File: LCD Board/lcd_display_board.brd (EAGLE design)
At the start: 47.2 x 39.3 mm, 26 parts, among them U1 ATMEGA328P_TQFP, Y1 16MHz

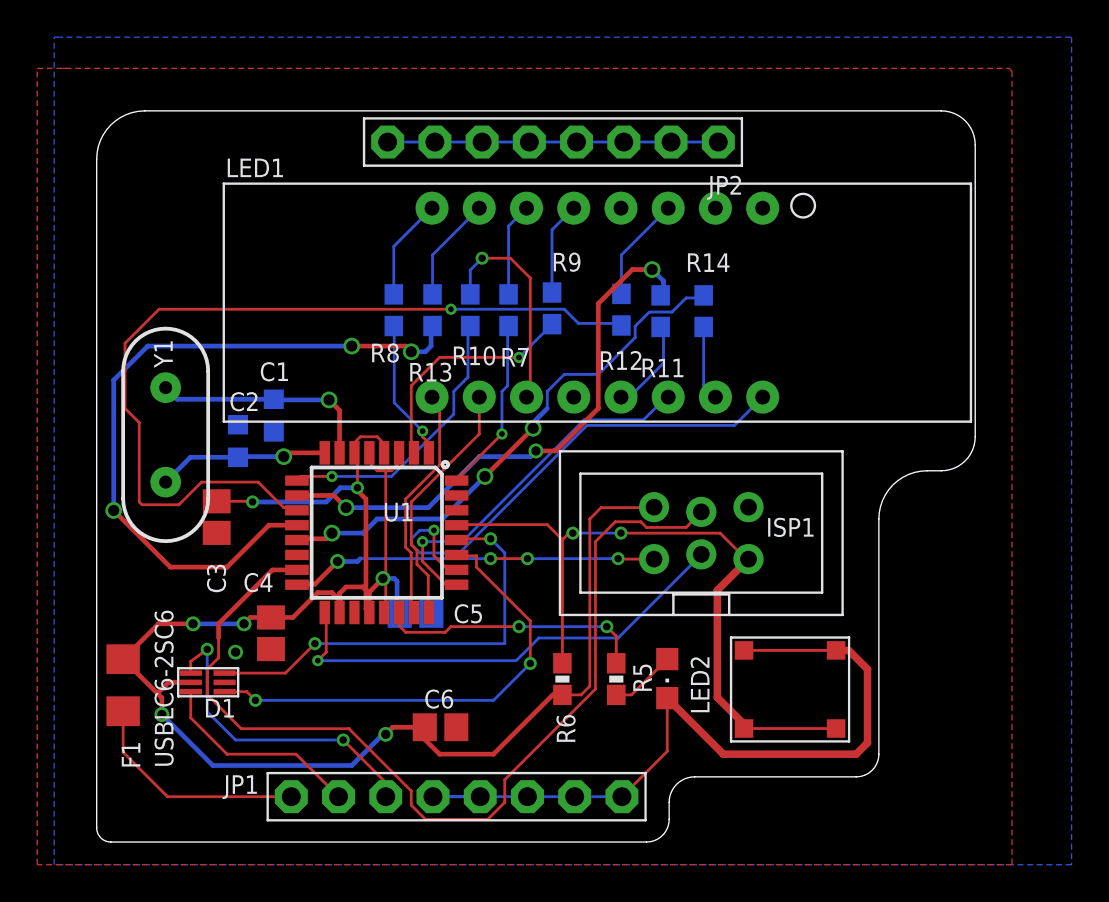
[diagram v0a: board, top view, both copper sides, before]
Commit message: fcc schematic mostly done
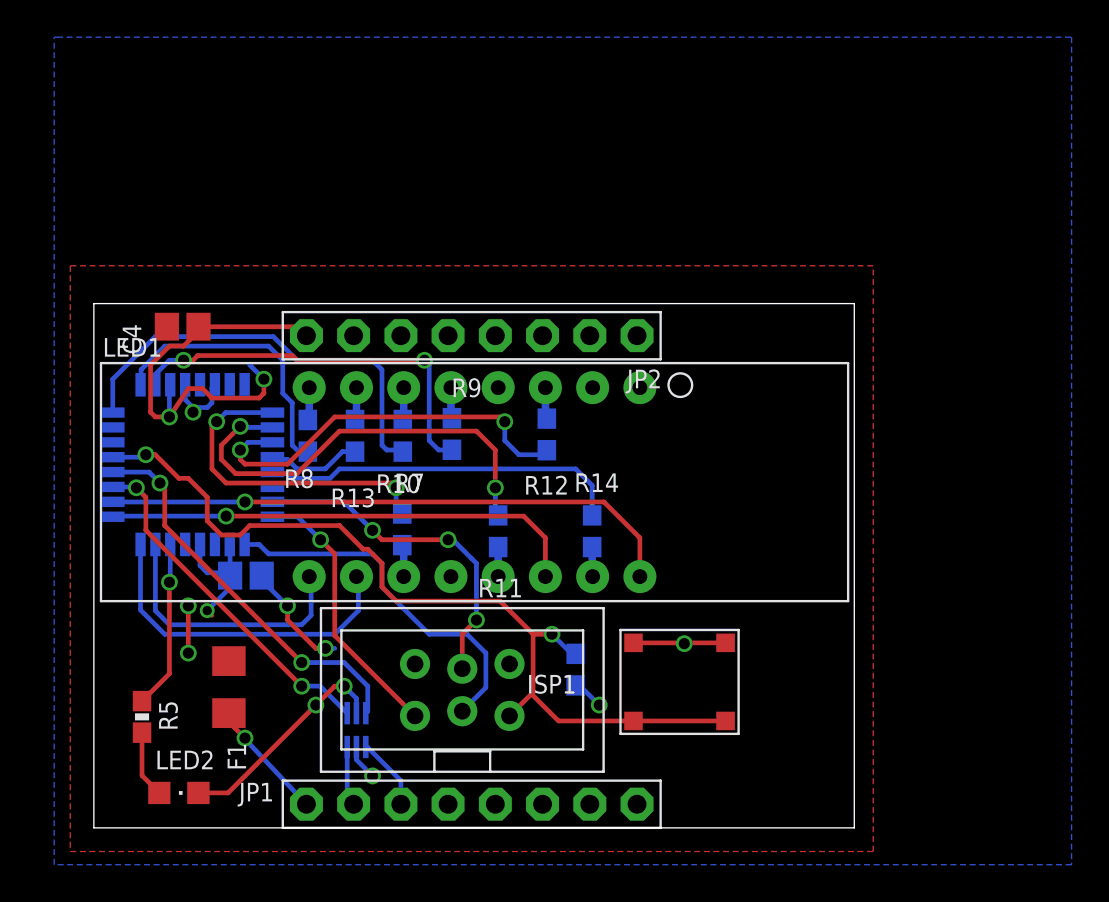
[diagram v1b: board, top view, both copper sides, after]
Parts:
- removed C1, C2: 22pF, adafruit:C0603K
- removed C5: 0.1uF, adafruit:C0805
- removed C6: 1uF, adafruit:C0805
- removed Y1: 16MHz, SparkFun-FreqCtrl:HC49US
- moved LED2 27.0 mm to (4.57, 1.88), turned to 270 degrees
- moved R5 25.6 mm to (2.59, 5.97)
- moved C4 17.2 mm to (4.78, 26.9), turned to 0 degrees
- moved ISP1 15.4 mm to (19.8, 7.42)
- moved R11 14.7 mm to (21.7, 16.0)
- moved R14 13.3 mm to (26.8, 16.0)
- moved R10 12.3 mm to (16.6, 16.1), turned to 270 degrees
- moved LED1 11.7 mm to (20.5, 18.6)
- moved JP2 11.3 mm to (20.3, 26.5)
- moved U1 10.6 mm to (5.31, 19.5), flipped to the bottom
- moved R7 8.83 mm to (16.6, 21.1)
- moved R9 8.64 mm to (19.3, 21.2)
- moved D1 8.40 mm to (14.1, 5.26), flipped to the bottom, turned to 180 degrees
- moved R8 8.19 mm to (11.5, 21.1)
- moved R13 7.94 mm to (14.0, 21.1)
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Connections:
- removed net +5V: C3.1, C4.1, C5.1, C6.1, D1.P$5, F1.1, ISP1.2, R6.2, U1.18, U1.20, U1.4, U1.6
- removed net N$1: C1.1, U1.7, Y1.2
- removed net N$2: C2.1, U1.8, Y1.1
- new net +3.3V: C3.1, C4.1, D1.P$5, F1.1, R6.2, U1.18, U1.20, U1.4, U1.6
- new net VCC: ISP1.2
- net GND: no longer C1.2, C2.2, C5.2, C6.2
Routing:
- net +5V: track 87.2 -> 0.00 mm, vias 7 -> 0
- net MOSI: track 52.3 -> 18.3 mm, vias 0 -> 3
- net N$15: track 38.3 -> 5.09 mm, vias 3 -> 0
- net N$14: track 46.4 -> 21.6 mm, vias 1 -> 2
- net GND: track 71.0 -> 49.2 mm, vias 1 -> 9
- net +3.3V: track 0.00 -> 15.6 mm, vias 0 -> 4
- net N$9: track 9.49 -> 23.3 mm, vias 1 -> 0
- net N$17: track 17.0 -> 3.91 mm, vias 2 -> 0
- net N$1: track 12.1 -> 0.00 mm, vias 1 -> 0
- net SEGD: track 11.7 -> 1.77 mm, vias 1 -> 0
- net N$2: track 9.21 -> 0.00 mm, vias 1 -> 0
- net N$16: track 28.5 -> 19.5 mm, vias 3 -> 0
- net N$11: track 12.6 -> 21.4 mm, vias 1 -> 2
- net ATM_RESET: track 38.8 -> 47.3 mm
- net N$6: track 11.1 -> 3.18 mm
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- added copper zone on layer 1, net +3.3V
- removed copper zone on layer 1, net GND
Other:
- board size 47.2 x 39.3 mm -> 40.9 x 28.2 mm

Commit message: cleaned up silk screens
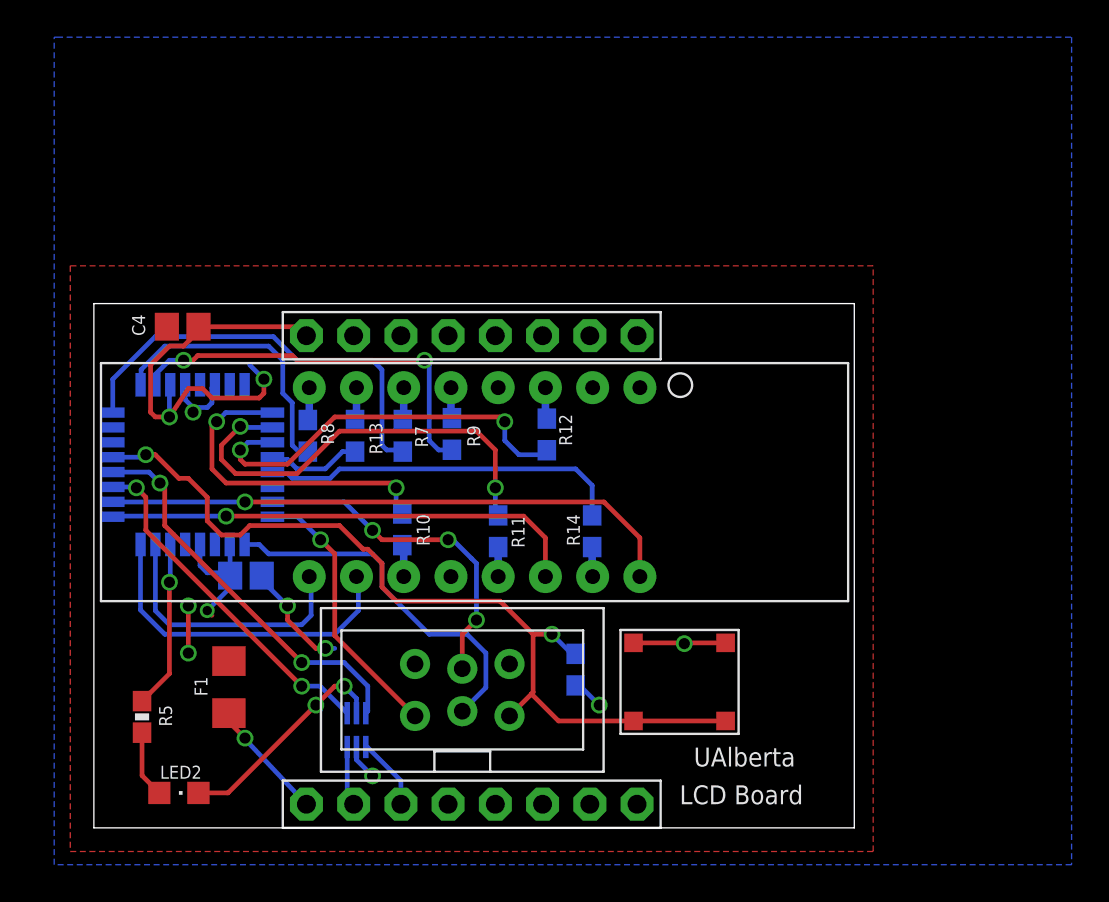
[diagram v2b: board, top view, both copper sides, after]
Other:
- board text added: "LCD Board"
- board text added: "UAlberta"
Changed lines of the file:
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@@
 <wire x1="40.894" y1="28.194" x2="0" y2="28.194" width="0" layer="20"/>
 <wire x1="0" y1="28.194" x2="0" y2="0" width="0" layer="20"/>
+<text x="32.258" y="3.302" size="1.016" layer="21" ratio="18">UAlberta</text>
+<text x="31.496" y="1.27" size="1.016" layer="21" ratio="18">LCD Board</text>
 </plain>
 <attributes>
@@
 <elements>
 <element name="C3" library="adafruit" package="C0805" value="1uF" x="8.1788" y="13.5636" smashed="yes" rot="MR180">
-<attribute name="NAME" x="10.6426" y="14.0716" size="1" layer="26" rot="MR180"/>
-<attribute name="VALUE" x="8.509" y="16.1544" size="1" layer="28" rot="MR180"/>
+<attribute name="NAME" x="8.8646" y="15.3416" size="0.7" layer="26" ratio="15" rot="MR180"/>
 </element>
 <element name="C4" library="adafruit" package="C0805" value="0.1uF" x="4.7752" y="26.9494" smashed="yes">
-<attribute name="NAME" x="1.5494" y="27.1018" size="1" layer="25" rot="R270"/>
-<attribute name="VALUE" x="7.8486" y="26.1874" size="1" layer="27" rot="R90"/>
+<attribute name="NAME" x="2.0574" y="27.6098" size="0.7" layer="25" ratio="15" rot="R270"/>
 </element>
 <element name="D1" library="USBLC6-2SC6" package="USBLC6-2SC6" value="USBLC6-2SC6" x="14.1224" y="5.2578" smashed="yes" rot="MR180">
-<attribute name="NAME" x="13.2334" y="6.7818" size="1" layer="22" rot="MR270"/>
-<attribute name="VALUE" x="18.0594" y="2.413" size="1" layer="22" rot="MR0"/>
+<attribute name="NAME" x="13.2334" y="6.0198" size="0.7" layer="22" ratio="15" rot="MR270"/>
 </element>
 <element name="F1" library="polyfuse" package="1206" value="" x="7.2644" y="7.5692" smashed="yes" rot="R270">
-<attribute name="NAME" x="7.1882" y="4.572" size="1" layer="25" rot="R270"/>
+<attribute name="NAME" x="5.4102" y="8.128" size="0.7" layer="25" ratio="15" rot="R270"/>
 <attribute name="VALUE" x="5.7404" y="8.9662" size="0.4064" layer="27" rot="R270"/>
 </element>
-<element name="ISP1" library="adafruit" package="AVRISP-BOX" value="AVRISP-BOX" x="19.812" y="7.4168" smashed="yes" rot="R90">
-<attribute name="NAME" x="25.9604" y="8.2268" size="1" layer="25" rot="R180"/>
-</element>
-<element name="LED1" library="SparkFun-Displays" package="7-SEGMENT-4DIGIT-YOUNGSUN" value="7-SEGMENT-4DIGIT-YOUNGSUN" x="20.4724" y="18.5928" smashed="yes">
-<attribute name="NAME" x="0.4724" y="25.3388" size="1" layer="25"/>
-<attribute name="VALUE" x="39.177" y="11.7084" size="1" layer="27" rot="R180"/>
-</element>
+<element name="ISP1" library="adafruit" package="AVRISP-BOX" value="AVRISP-BOX" x="19.812" y="7.4168" smashed="yes" rot="R90"/>
+<element name="LED1" library="SparkFun-Displays" package="7-SEGMENT-4DIGIT-YOUNGSUN" value="7-SEGMENT-4DIGIT-YOUNGSUN" x="20.4724" y="18.5928" smashed="yes"/>
 <element name="LED2" library="adafruit" package="CHIPLED_0805" value="" x="4.572" y="1.8796" smashed="yes" rot="R270">
-<attribute name="NAME" x="3.302" y="3.1496" size="1" layer="25"/>
+<attribute name="NAME" x="3.556" y="2.6416" size="0.7" layer="25" ratio="15"/>
 <attribute name="VALUE" x="3.302" y="-0.6604" size="1.27" layer="27"/>
 </element>
 <element name="R10" library="SparkFun-Resistors" package="0603-RES" value="80 Ohm" x="16.5862" y="16.0528" smashed="yes" rot="MR270">
-<attribute name="NAME" x="15.1638" y="18.0086" size="1" layer="25" font="vector" ratio="11"/>
-<attribute name="VALUE" x="17.272" y="17.0688" size="1" layer="27" font="vector" ratio="11" rot="R270"/>
+<attribute name="NAME" x="18.0594" y="15.1638" size="0.7" layer="25" font="vector" ratio="15" rot="R90"/>
 </element>
 <element name="R11" library="SparkFun-Resistors" package="0603-RES" value="80 Ohm" x="21.7424" y="15.9512" smashed="yes" rot="MR270">
-<attribute name="NAME" x="20.6502" y="12.3952" size="1" layer="25" font="vector" ratio="11"/>
-<attribute name="VALUE" x="20.2946" y="19.8628" size="1" layer="27" font="vector" ratio="11" rot="R270"/>
+<attribute name="NAME" x="23.1648" y="15.0622" size="0.7" layer="25" font="vector" ratio="15" rot="R90"/>
 </element>
 <element name="R12" library="SparkFun-Resistors" package="0603-RES" value="80 Ohm" x="24.3586" y="21.1582" smashed="yes" rot="MR90">
-<attribute name="NAME" x="25.5524" y="18.923" size="1" layer="25" font="vector" ratio="11" rot="R180"/>
-<attribute name="VALUE" x="23.5204" y="19.5326" size="1" layer="27" font="vector" ratio="11" rot="R90"/>
+<attribute name="NAME" x="25.019" y="22.2504" size="0.7" layer="25" font="vector" ratio="15" rot="R270"/>
 </element>
 <element name="R13" library="SparkFun-Resistors" package="0603-RES" value="80 Ohm" x="14.0462" y="21.082" smashed="yes" rot="MR90">
-<attribute name="NAME" x="12.7254" y="17.2466" size="1" layer="25" font="vector" ratio="11"/>
-<attribute name="VALUE" x="13.5128" y="20.066" size="1" layer="27" font="vector" ratio="11" rot="R90"/>
+<attribute name="NAME" x="15.5194" y="20.0914" size="0.7" layer="25" font="vector" ratio="15" rot="R90"/>
 </element>
 <element name="R14" library="SparkFun-Resistors" package="0603-RES" value="80 Ohm" x="26.797" y="15.9512" smashed="yes" rot="MR270">
-<attribute name="NAME" x="25.8318" y="18.0594" size="1" layer="25" font="vector" ratio="11"/>
-<attribute name="VALUE" x="27.6352" y="18.034" size="1" layer="27" font="vector" ratio="11" rot="R270"/>
+<attribute name="NAME" x="26.1366" y="15.1638" size="0.7" layer="25" font="vector" ratio="15" rot="R90"/>
 </element>
 <element name="R5" library="SparkFun-Resistors" package="0603-RES" value="1k" x="2.5908" y="5.969" smashed="yes" rot="R270">
-<attribute name="NAME" x="3.5052" y="6.858" size="1" layer="25" font="vector" ratio="11" rot="R270"/>
-<attribute name="VALUE" x="2.0574" y="3.937" size="1" layer="27" font="vector" ratio="11" rot="R270"/>
+<attribute name="NAME" x="3.5052" y="6.604" size="0.7" layer="25" font="vector" ratio="15" rot="R270"/>
 </element>
 <element name="R6" library="SparkFun-Resistors" package="0603-RES" value="10k" x="25.908" y="8.509" smashed="yes" rot="MR270">
-<attribute name="NAME" x="26.2128" y="6.6548" size="1" layer="26" font="vector" ratio="11" rot="MR270"/>
-<attribute name="VALUE" x="27.9654" y="8.4582" size="1" layer="28" font="vector" ratio="11" rot="MR270"/>
+<attribute name="NAME" x="24.9428" y="9.4488" size="0.7" layer="26" font="vector" ratio="15" rot="MR270"/>
 </element>
 <element name="R7" library="SparkFun-Resistors" package="0603-RES" value="80 Ohm" x="16.6116" y="21.082" smashed="yes" rot="MR90">
-<attribute name="NAME" x="17.8054" y="19.05" size="1" layer="25" font="vector" ratio="11" rot="R180"/>
-<attribute name="VALUE" x="16.0782" y="20.066" size="1" layer="27" font="vector" ratio="11" rot="R90"/>
+<attribute name="NAME" x="17.272" y="21.6154" size="0.7" layer="25" font="vector" ratio="15" rot="R270"/>
 </element>
 <element name="R8" library="SparkFun-Resistors" package="0603-RES" value="80 Ohm" x="11.5062" y="21.082" smashed="yes" rot="MR90">
-<attribute name="NAME" x="11.8618" y="19.2786" size="1" layer="25" font="vector" ratio="11" rot="R180"/>
-<attribute name="VALUE" x="10.3632" y="20.066" size="1" layer="27" font="vector" ratio="11" rot="R90"/>
+<attribute name="NAME" x="12.2174" y="21.7678" size="0.7" layer="25" font="vector" ratio="15" rot="R270"/>
 </element>
 <element name="R9" library="SparkFun-Resistors" package="0603-RES" value="80 Ohm" x="19.2532" y="21.1836" smashed="yes" rot="MR90">
-<attribute name="NAME" x="19.2278" y="23.1648" size="1" layer="25" font="vector" ratio="11"/>
-<attribute name="VALUE" x="18.7198" y="19.1008" size="1" layer="27" font="vector" ratio="11" rot="R90"/>
+<attribute name="NAME" x="20.7772" y="20.4978" size="0.7" layer="25" font="vector" ratio="15" rot="R90"/>
 </element>
 <element name="U$10" library="EG4621CT-ND" package="EG4621CT-ND" value="EG4621CT-ND" x="31.496" y="7.8486" smashed="yes"/>
 <element name="U1" library="SparkFun-DigitalIC" package="TQFP32-08" value="ATMEGA328P_TQFP" x="5.3086" y="19.5326" smashed="yes" rot="MR270">
 <attribute name="PROD_ID" value="IC-09069" x="5.3086" y="19.5326" size="1.778" layer="28" rot="MR270" display="off"/>
-<attribute name="NAME" x="4.9784" y="20.1422" size="1" layer="26" rot="MR0"/>
-<attribute name="VALUE" x="13.335" y="11.9634" size="1" layer="28" rot="MR0"/>
 </element>
 <element name="JP1" library="adafruit" package="1X08-BIG" value="" x="20.32" y="1.27" smashed="yes">
-<attribute name="NAME" x="7.7978" y="1.4224" size="1" layer="25" ratio="10"/>
 <attribute name="VALUE" x="10.16" y="-1.905" size="1.27" layer="27"/>
 </element>
 <element name="JP2" library="adafruit" package="1X08-BIG" value="" x="20.32" y="26.4668" smashed="yes" rot="R180">
-<attribute name="NAME" x="30.5562" y="24.638" size="1" layer="25" ratio="10" rot="R180"/>
 <attribute name="VALUE" x="30.48" y="29.6418" size="1.27" layer="27" rot="R180"/>
 </element>
